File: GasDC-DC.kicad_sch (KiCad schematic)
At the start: 22 parts, among them IC1 TPS56637RPAR, J1 Conn_01x02, Q1 2N7002_SOT-23-3

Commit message: fix
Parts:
- removed R8: R_1k_0201, Hardware Components Footprints:R_0201, symbol lib:R_1k_0201
- added R16: R_1k_0402, Hardware Components Footprints:R_0402_1005Metric, symbol Hardware Components:R_1k_0402
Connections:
- net +16V: now also R16.2
- net at D1.2 (A): now also R16.1
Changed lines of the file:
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@@
+	)
+	(symbol
+		(lib_id "Hardware Components:R_1k_0402")
+		(at 228.6 83.82 90)
+		(unit 1)
+		(exclude_from_sim no)
+		(in_bom yes)
+		(on_board yes)
+		(dnp no)
+		(fields_autoplaced yes)
+		(property "Reference" "R16"
+			(at 231.14 80.01 90)
+			(effects
+				(font
+					(size 1.27 1.27)
+					(thickness 0.15)
+				)
+				(justify right)
+			)
+		)
+		(property "Value" "R_1k_0402"
+			(at 241.3 63.5 0)
+			(effects
+				(font
+					(size 1.27 1.27)
+					(thickness 0.15)
+				)
+				(justify left bottom)
+				(hide yes)
+			)
+		)
+		(property "Footprint" "Hardware Components Footprints:R_0402_1005Metric"
+			(at 243.84 63.5 0)
+			(effects
+				(font
+					(size 1.27 1.27)
+					(thickness 0.15)
+				)
+				(justify left bottom)
+				(hide yes)
+			)
+		)
+		(property "Datasheet" "https://www.bourns.com/docs/product-datasheets/cr.pdf"
+			(at 246.38 63.5 0)
+			(effects
+				(font
+					(size 1.27 1.27)
+					(thickness 0.15)
+				)
+				(justify left bottom)
+				(hide yes)
+			)
+		)
+		(property "Description" "SMD Chip Resistor, 1 kohm, ± 1%, 63 mW, 0402 [1005 Metric], Thick Film, General Purpose"
+			(at 228.6 83.82 0)
+			(effects
+				(font
+					(size 1.27 1.27)
+				)
+				(hide yes)
+			)
+		)
+		(property "MPN" "CR0402-FX-1001GLF"
+			(at 248.92 63.5 0)
+			(effects
+				(font
+					(size 1.27 1.27)
+					(thickness 0.15)
+				)
+				(justify left bottom)
+				(hide yes)
+			)
+		)
+		(property "Manufacturer" "Bourns"
+			(at 251.46 63.5 0)
+			(effects
+				(font
+					(size 1.27 1.27)
+					(thickness 0.15)
+				)
+				(justify left bottom)
+				(hide yes)
+			)
+		)
+		(property "License" "Apache-2.0"
+			(at 254 63.5 0)
+			(effects
+				(font
+					(size 1.27 1.27)
+					(thickness 0.15)
+				)
+				(justify left bottom)
+				(hide yes)
+			)
+		)
+		(property "Author" "Antmicro"
+			(at 256.54 63.5 0)
+			(effects
+				(font
+					(size 1.27 1.27)
+					(thickness 0.15)
+				)
+				(justify left bottom)
+				(hide yes)
+			)
+		)
+		(property "Val" "1k"
+			(at 231.14 82.55 90)
+			(effects
+				(font
+					(size 1.27 1.27)
+					(thickness 0.15)
+				)
+				(justify right)
+			)
+		)
+		(property "Tolerance" "1%"
+			(at 238.76 63.5 0)
+			(effects
+				(font
+					(size 1.27 1.27)
+				)
+				(justify left bottom)
+				(hide yes)
+			)
+		)
+		(pin "1"
+		)
+		(pin "2"
+		)
+		(instances
+			(project "robot-pmu-hw"
+				(path "/ca7f4c4c-3c96-472a-b66f-ec124f8cf9b5/ba29ec8f-07b0-421f-8a8f-2bec5c180b4e"
+					(reference "R16")
+					(unit 1)
+				)
+			)
+		)
 	)
 	(symbol
@@
 					(unit 1)
 				)
-			)
-		)
-	)
-	(symbol
-		(lib_id "lib:R_1k_0201")
-		(at 228.6 83.82 90)
-		(unit 1)
-		(exclude_from_sim no)
-		(in_bom yes)
-		(on_board yes)
-		(dnp no)
-		(fields_autoplaced yes)
-		(property "Reference" "R8"
-			(at 231.14 80.01 90)
-			(effects
-				(font
-					(size 1.27 1.27)
-					(thickness 0.15)
-				)
-				(justify right)
-			)
-		)
-		(property "Value" "R_1k_0201"
-			(at 241.3 68.58 0)
-			(effects
-				(font
-					(size 1.27 1.27)
-					(thickness 0.15)
-				)
-				(justify left bottom)
-				(hide yes)
-			)
-		)
-		(property "Footprint" "Hardware Components Footprints:R_0201"
-			(at 243.84 68.58 0)
-			(effects
-				(font
-					(size 1.27 1.27)
-					(thickness 0.15)
-				)
-				(justify left bottom)
-				(hide yes)
-			)
-		)
-		(property "Datasheet" "https://www.bourns.com/docs/product-datasheets/cr.pdf"
-			(at 246.38 68.58 0)
-			(effects
-				(font
-					(size 1.27 1.27)
-					(thickness 0.15)
-				)
-				(justify left bottom)
-				(hide yes)
-			)
-		)
-		(property "Description" "1 kOhms ±1% 0.05W, 1/20W, Chip Resistor 0402 (1005 Metric) Thick Film"
-			(at 228.6 83.82 0)
-			(effects
-				(font
-					(size 1.27 1.27)
-				)
-				(hide yes)
-			)
-		)
-		(property "MPN" "CR0201-FX-1001GLF"
-			(at 248.92 68.58 0)
-			(effects
-				(font
-					(size 1.27 1.27)
-					(thickness 0.15)
-				)
-				(justify left bottom)
-				(hide yes)
-			)
-		)
-		(property "Manufacturer" "Bourns"
-			(at 251.46 68.58 0)
-			(effects
-				(font
-					(size 1.27 1.27)
-					(thickness 0.15)
-				)
-				(justify left bottom)
-				(hide yes)
-			)
-		)
-		(property "License" "Apache-2.0"
-			(at 254 68.58 0)
-			(effects
-				(font
-					(size 1.27 1.27)
-					(thickness 0.15)
-				)
-				(justify left bottom)
-				(hide yes)
-			)
-		)
-		(property "Author" "Antmicro"
-			(at 256.54 68.58 0)
-			(effects
-				(font
-					(size 1.27 1.27)
-					(thickness 0.15)
-				)
-				(justify left bottom)
-				(hide yes)
-			)
-		)
-		(property "Val" "1k"
-			(at 231.14 82.55 90)
-			(effects
-				(font
-					(size 1.27 1.27)
-					(thickness 0.15)
-				)
-				(justify right)
-			)
-		)
-		(property "Tolerance" "1%"
-			(at 238.76 68.58 0)
-			(effects
-				(font
-					(size 1.27 1.27)
-					(thickness 0.15)
-				)
-				(justify left bottom)
-				(hide yes)
-			)
-		)
-		(property "LCSC" ""
-			(at 228.6 83.82 90)
-			(effects
-				(font
-					(size 1.27 1.27)
-				)
-				(hide yes)
-			)
-		)
-		(pin "2"
-		)
-		(pin "1"
-		)
-		(instances
-			(project ""
-				(path "/ca7f4c4c-3c96-472a-b66f-ec124f8cf9b5/ba29ec8f-07b0-421f-8a8f-2bec5c180b4e"
-					(reference "R8")
-					(unit 1)
-				)

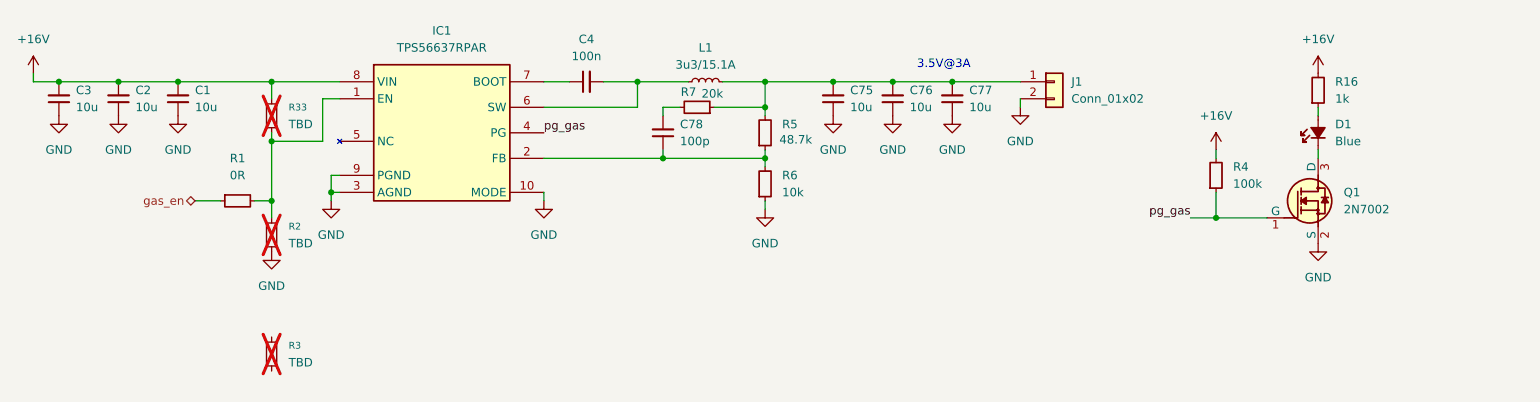
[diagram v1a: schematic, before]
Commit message: Adjustable output
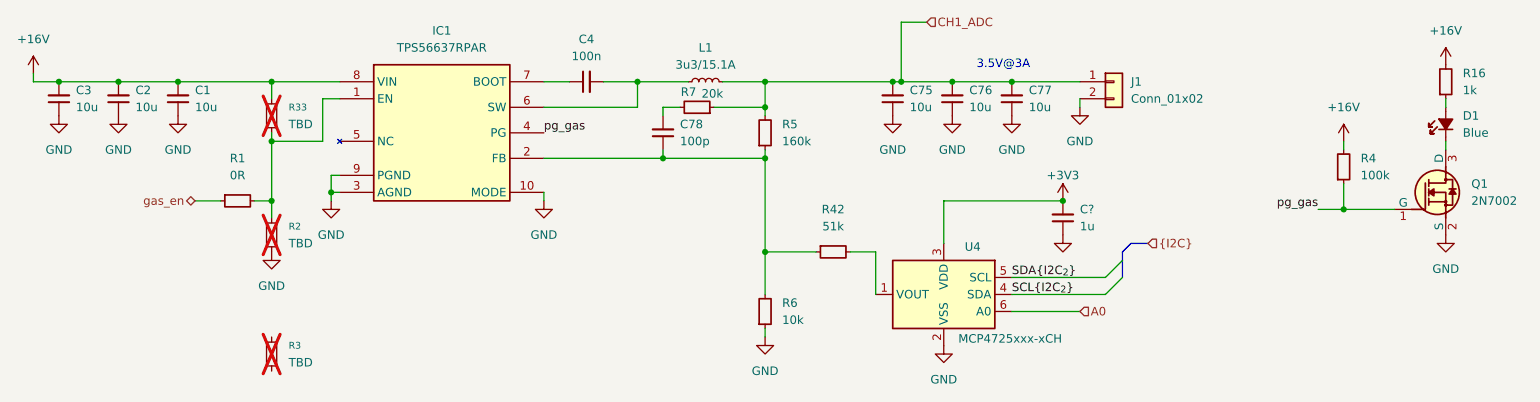
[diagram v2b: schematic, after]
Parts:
- removed R5: R_48k7_0402, Hardware Components Footprints:R_0402_1005Metric, symbol Hardware Components:R_4k7_0402
- added C?: C_1u_0402, Hardware Components Footprints:C_0402_1005Metric, symbol lib:C_1u_0402
- added R42: R_51k_0402, Hardware Components Footprints:R_0402_1005Metric, symbol Hardware Components:R_51k_0402
- added R5: R_160k_0402, Hardware Components Footprints:R_0402_1005Metric, symbol Hardware Components:R_160k_0402
- added U4: MCP4725xxx-xCH, Package_TO_SOT_SMD:SOT-23-6, symbol Analog_DAC:MCP4725xxx-xCH
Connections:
- net GND: now also C?.1, U4.2 (VSS)
- net CH1_ADC: now reaches C75.2, C76.2, C77.2, J1.1 (Pin_1), L1.2, R7.1
- net CH1_ADC: now also R5.2
- net at C78.1, IC1.2 (FB), R6.2: now also R42.1, R5.1
- new net: R42.2, U4.1 (VOUT)
- new net +3V3: C?.2, U4.3 (VDD)
- new net A0: U4.6 (A0)
- new net SCL{I2C_{2}}: U4.4 (SDA)
- new net SDA{I2C_{2}}: U4.5 (SCL)
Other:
- moved on the sheet: C75, C76, C77, D1, J1, Q1, R16, R4, R6
